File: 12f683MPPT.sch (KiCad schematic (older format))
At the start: 46 parts, among them J1 Conn_01x01_Male, J2 Conn_01x01_Male, J3 Conn_01x01_Male, J4 Conn_01x01_Male, Q1 BUK9511-55A127, Q2 BUK9511-55A127, Q3 2N2222A, Q4 2N2222A, Q5 2N2907A, SW1 SW_Push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

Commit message: Add zener diode for FET protection.
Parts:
- added D9: 1N5733A 5.1V, Diode_THT:D_DO-41_SOD81_P10.16mm_Horizontal, symbol Device:D_Zener
- Q1, Q2: footprint TO_SOT_Packages_THT:TO-220-3_Vertical -> Package_TO_SOT_THT:TO-220-3_Vertical
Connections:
- net at Q2.1 (G), Q4.1 (E), Q5.1 (E): now also D9.1 (K)
- net at C2.2, D1.2 (A), Q2.3 (S)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: now also D9.2 (A)
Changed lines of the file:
@@
 EESchema Schematic File Version 4
-LIBS:12f683MPPT-cache
-EELAYER 29 0
+EELAYER 30 0
 EELAYER END
 $Descr A4 11693 8268
@@
 F 0 "Q1" H 8800 5300 50  0000 R CNN
 F 1 "BUK9511-55A127" H 9400 5200 50  0000 R CNN
-F 2 "TO_SOT_Packages_THT:TO-220-3_Vertical" H 8700 5400 29  0001 C CNN
+F 2 "Package_TO_SOT_THT:TO-220-3_Vertical" H 8700 5400 29  0001 C CNN
 F 3 "" H 8500 5300 60  0000 C CNN
 	1    8500 5300
@@
 F 0 "Q2" V 7650 2550 50  0000 R CNN
 F 1 "BUK9511-55A127" V 7750 2600 50  0000 R CNN
-F 2 "TO_SOT_Packages_THT:TO-220-3_Vertical" H 7650 2400 29  0001 C CNN
+F 2 "Package_TO_SOT_THT:TO-220-3_Vertical" H 7650 2400 29  0001 C CNN
 F 3 "" H 7450 2300 60  0000 C CNN
 	1    7450 2300
@@
 	7750 2200 7900 2200
 Wire Wire Line
-	7250 3500 7750 3500
+	7250 3500 7450 3500
 Wire Wire Line
 	5850 5600 5550 5600
@@
 	2250 1200 2100 1200
 Connection ~ 2100 1200
+$Comp
+L Device:D_Zener D9
+U 1 1 608BF065
+P 7450 3300
+F 0 "D9" V 7404 3380 50  0000 L CNN
+F 1 "1N5733A 5.1V" V 7495 3380 50  0000 L CNN
+F 2 "Diode_THT:D_DO-41_SOD81_P10.16mm_Horizontal" H 7450 3300 50  0001 C CNN
+F 3 "~" H 7450 3300 50  0001 C CNN
+	1    7450 3300
+	0    1    1    0
+$EndComp
+Wire Wire Line
+	7450 3450 7450 3500
+Connection ~ 7450 3500
+Wire Wire Line
+	7450 3500 7750 3500
+Wire Wire Line
+	7450 3150 7450 3050
+Connection ~ 7450 3050
 $EndSCHEMATC

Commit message: R9 -> 2.2k
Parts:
- R9: value 10k -> 2.2k
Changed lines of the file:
@@
 Sheet 1 1
 Title "Simple MPPT with 12F683"
-Date "2019-05-19"
-Rev "1.0"
+Date "2021-05-07"
+Rev "1.1"
 Comp ""
 Comment1 ""
@@
 P 5850 2500
 F 0 "R9" V 5930 2500 50  0000 C CNN
-F 1 "10k" V 5850 2500 50  0000 C CNN
+F 1 "2.2k" V 5850 2500 50  0000 C CNN
 F 2 "Resistors_THT:R_Axial_DIN0309_L9.0mm_D3.2mm_P12.70mm_Horizontal" V 5780 2500 30  0001 C CNN
 F 3 "" H 5850 2500 30  0000 C CNN

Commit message: Update PCB.
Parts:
- SW1: footprint Buttons_Switches_THT:SW_PUSH_6mm_h7.3mm -> Button_Switch_THT:SW_PUSH_6mm_H7.3mm
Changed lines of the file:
@@
 F 0 "SW1" H 3050 5185 50  0000 C CNN
 F 1 "SW_Push" H 3050 5094 50  0000 C CNN
-F 2 "Buttons_Switches_THT:SW_PUSH_6mm_h7.3mm" H 3050 5100 50  0001 C CNN
+F 2 "Button_Switch_THT:SW_PUSH_6mm_H7.3mm" H 3050 5100 50  0001 C CNN
 F 3 "~" H 3050 5100 50  0001 C CNN
 	1    3050 4900

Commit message: C2 -> 4.7uF
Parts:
- C2: value 10u 50v -> 4.7u 50v
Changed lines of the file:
@@
 P 7250 2750
 F 0 "C2" H 7275 2850 50  0000 L CNN
-F 1 "10u 50v" H 7275 2650 50  0000 L CNN
+F 1 "4.7u 50v" H 7275 2650 50  0000 L CNN
 F 2 "Capacitors_THT:CP_Radial_D12.5mm_P5.00mm" H 7288 2600 30  0001 C CNN
 F 3 "" H 7250 2750 60  0000 C CNN

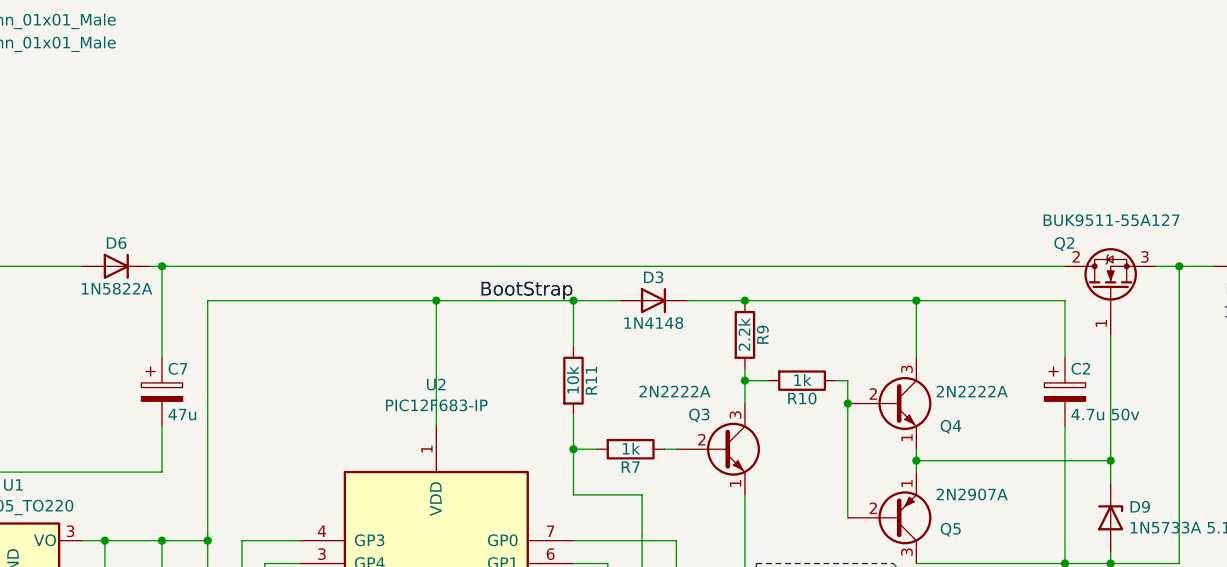
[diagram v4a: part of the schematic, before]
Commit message: Try to fix low bootstrap voltage.
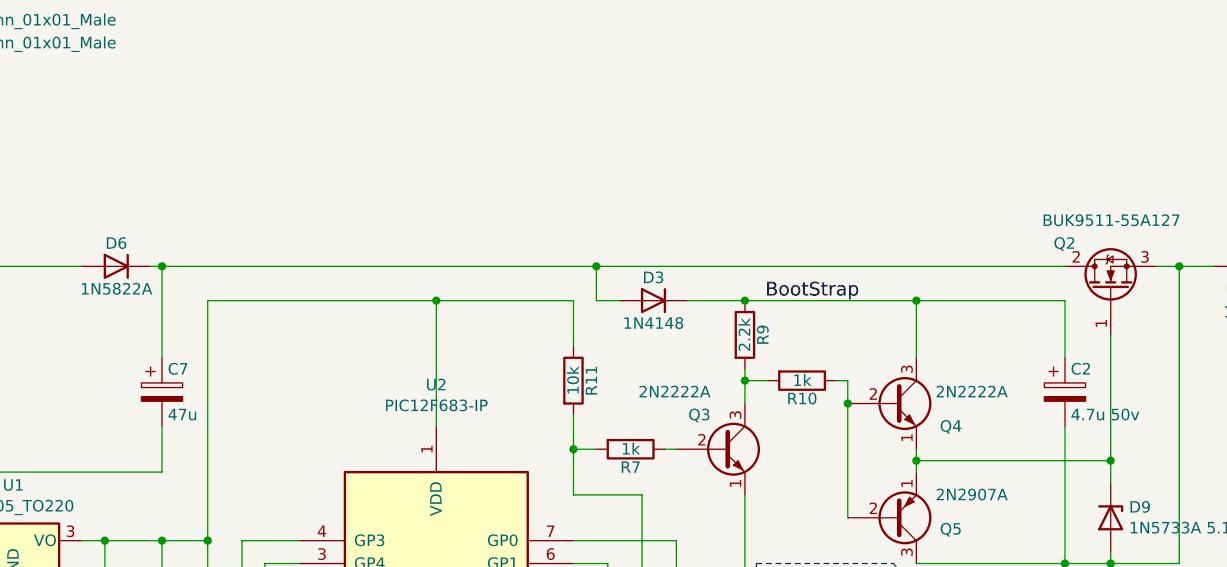
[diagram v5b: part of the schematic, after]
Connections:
- net BootStrap: now also C2.1, D3.1 (K), Q4.3 (C), R9.1; no longer C3.1, C4.1, D3.2 (A), R11.1, R14.1, R16.2, U1.3 (VO), U2.1 (VDD), U3.8 (V+)
- net at C7.1, D6.1 (K), Q2.2 (D): now also D3.2 (A)
- new net: C3.1, C4.1, R11.1, R14.1, R16.2, U1.3 (VO), U2.1 (VDD), U3.8 (V+)
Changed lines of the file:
@@
 	1    0    0    -1
 $EndComp
-Text Label 5100 2350 2    60   ~ 0
+Text Label 6350 2350 2    60   ~ 0
 BootStrap
 Text Label 7050 3600 2    60   ~ 0
@@
 Connection ~ 5850 2350
 Wire Wire Line
-	5300 2350 5100 2350
-Wire Wire Line
 	6250 2700 6300 2700
 Connection ~ 6300 2800
@@
 Wire Wire Line
 	5100 2350 5100 2550
-Connection ~ 5100 2350
 Wire Wire Line
 	5100 2350 4500 2350
@@
 Connection ~ 8400 5600
 Wire Wire Line
-	3300 2200 7250 2200
+	3300 2200 5200 2200
 Wire Wire Line
 	2250 2850 2250 3400
@@
 	7450 3150 7450 3050
 Connection ~ 7450 3050
+Wire Wire Line
+	5300 2350 5200 2350
+Wire Wire Line
+	5200 2350 5200 2200
+Connection ~ 5200 2200
+Wire Wire Line
+	5200 2200 7250 2200
 $EndSCHEMATC
